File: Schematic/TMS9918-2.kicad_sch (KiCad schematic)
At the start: 19 parts, among them J7 Power, J8 Video out, Q1 BC547, U11 TMS9918A, U12 HM62256BLP, U13 74HCT574, U14 74HCT574, U15 74HCT574, U9 74HCT04, Y1 10.738635MHz

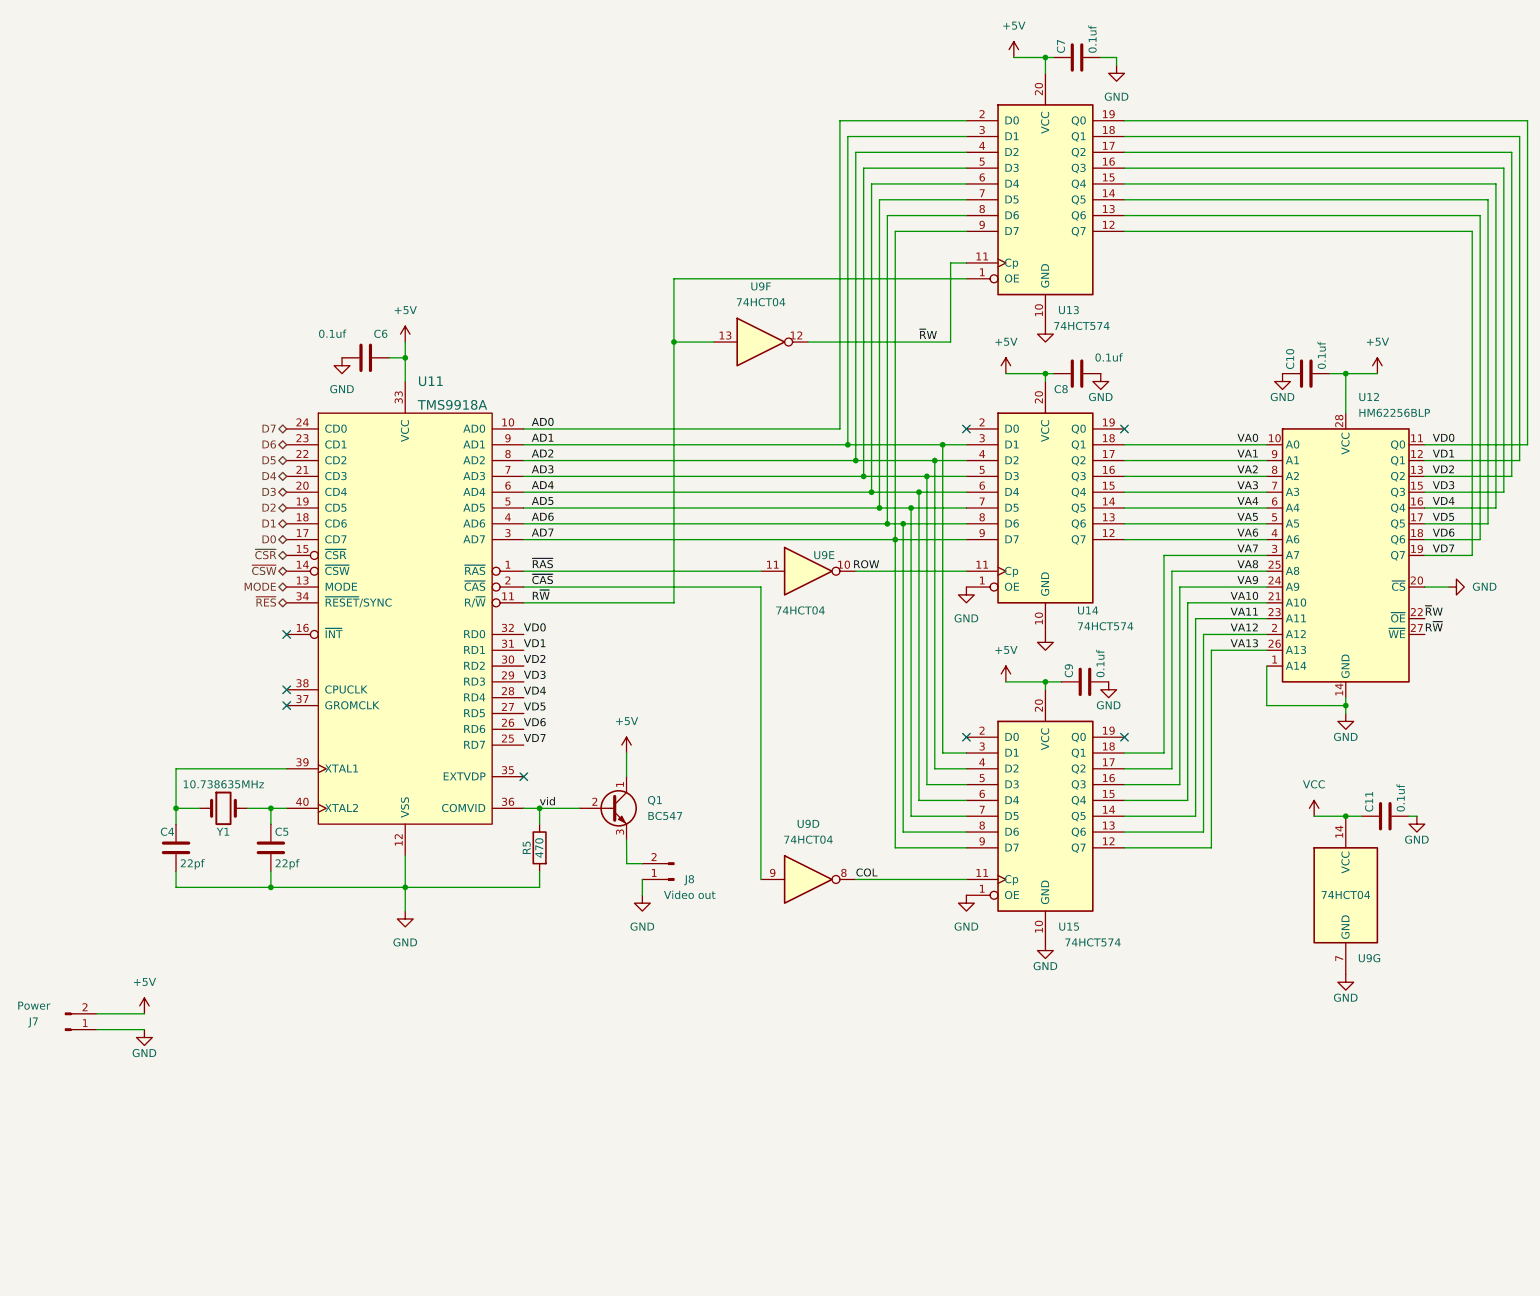
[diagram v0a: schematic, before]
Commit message: Update TMS9918-2.kicad_sch
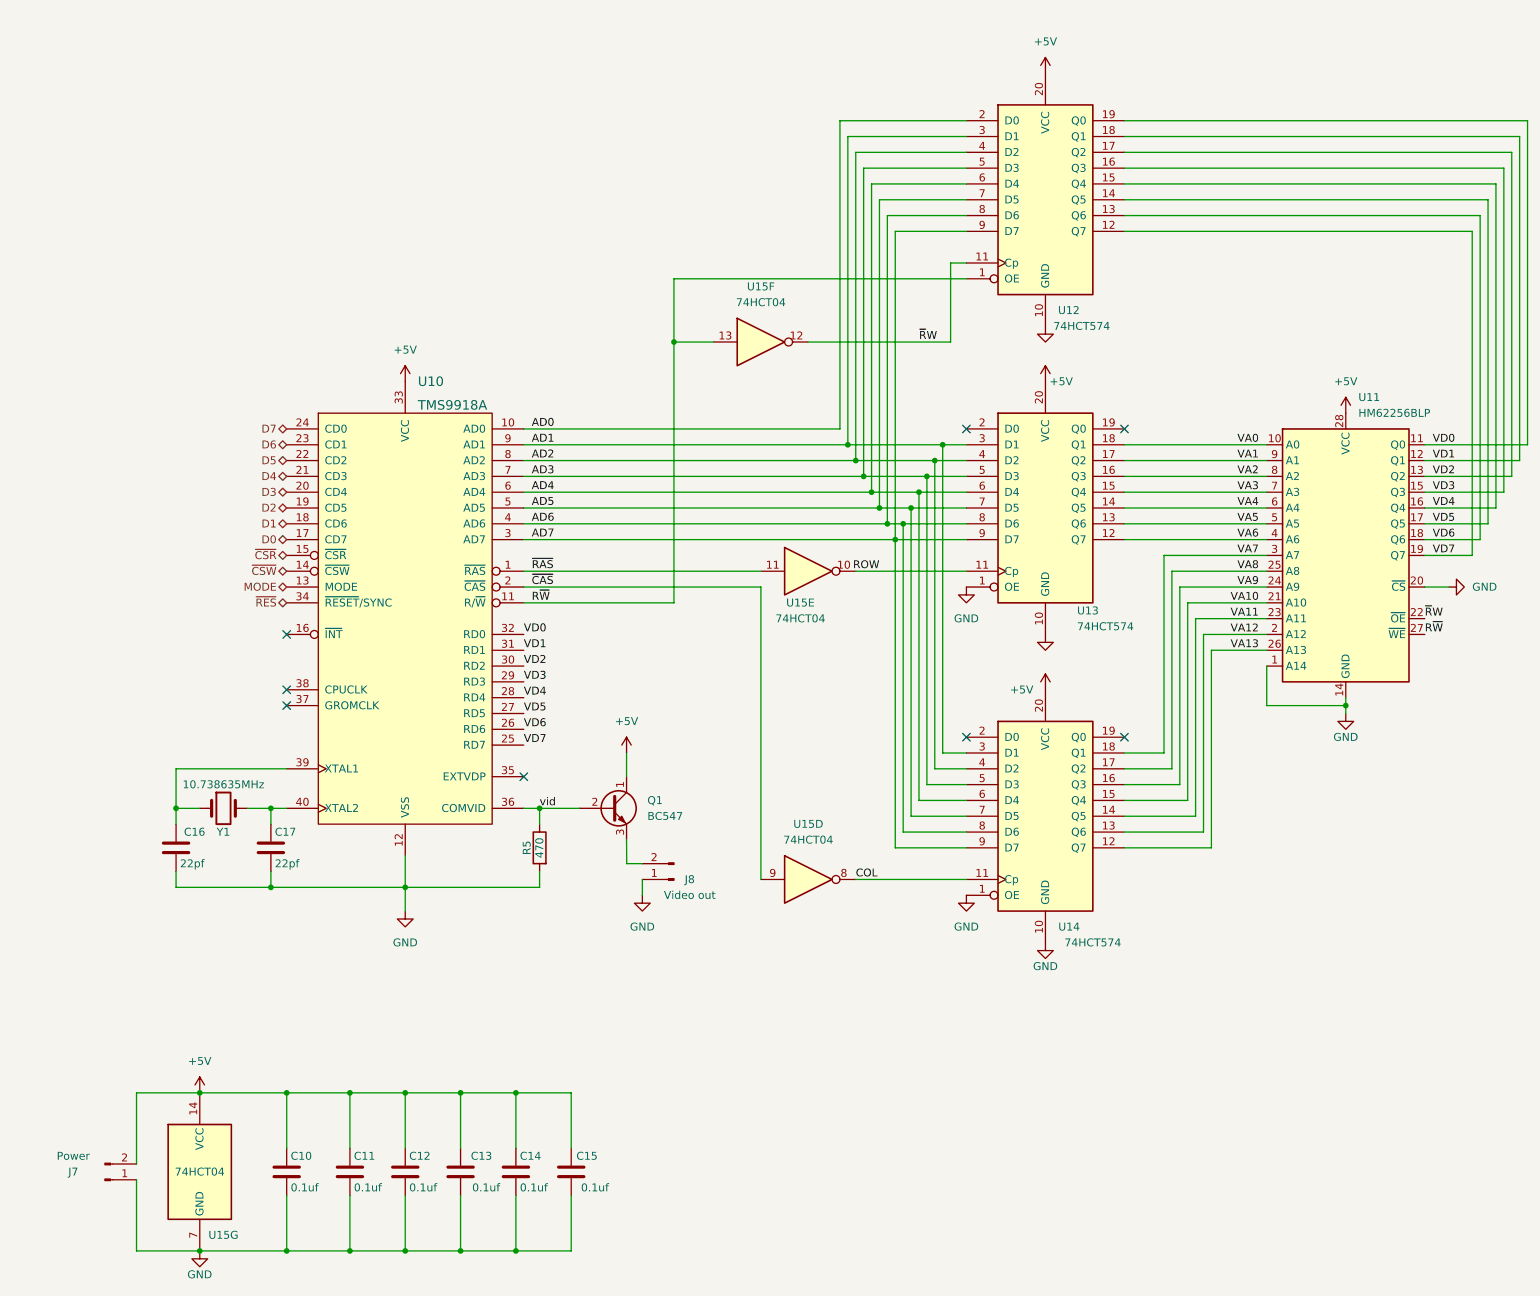
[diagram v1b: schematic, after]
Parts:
- renumbered C7 to C10, C10 to C11, C11 to C12, C6 to C13, C9 to C14, C8 to C15, C4 to C16, C5 to C17, U11 to U10, U12 to U11, U13 to U12, U14 to U13, U15 to U14, U9 to U15
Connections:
- net +5V: now also C11.1, C13.2; no longer C11.2, C13.1
- net GND: now also C11.2, C13.1; no longer C11.1, C13.2
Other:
- moved on the sheet: C10, C11, C12, C13, C14, C15, J7, U15G
